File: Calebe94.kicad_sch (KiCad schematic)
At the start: 107 parts, among them J1 USB_B, SW1 SW_DIP_x01, SW10 SW_DIP_x01, SW11 SW_DIP_x01, SW12 SW_DIP_x01, SW13 SW_DIP_x01, SW14 SW_DIP_x01, SW15 SW_DIP_x01, SW16 SW_DIP_x01, SW17 SW_DIP_x01, SW18 SW_DIP_x01, SW19 SW_DIP_x01, SW2 SW_DIP_x01, SW20 SW_DIP_x01, SW21 SW_DIP_x01, SW22 SW_DIP_x01, SW23 SW_DIP_x01, SW24 SW_DIP_x01, SW25 SW_DIP_x01, SW26 SW_DIP_x01, SW27 SW_DIP_x01, SW28 SW_DIP_x01, SW29 SW_DIP_x01, SW3 SW_DIP_x01, SW30 SW_DIP_x01, SW31 SW_DIP_x01, SW32 SW_DIP_x01, SW33 SW_DIP_x01, SW34 SW_DIP_x01, SW35 SW_DIP_x01, SW36 SW_DIP_x01, SW37 SW_DIP_x01, SW38 SW_DIP_x01, SW39 SW_DIP_x01, SW4 SW_DIP_x01, SW40 SW_DIP_x01, SW41 SW_DIP_x01, SW42 SW_DIP_x01, SW43 SW_DIP_x01, SW44 SW_DIP_x01, SW45 SW_DIP_x01, SW46 SW_DIP_x01, SW47 SW_DIP_x01, SW48 SW_DIP_x01, SW49 RESET, SW5 SW_DIP_x01, SW50 BOOT, SW6 SW_DIP_x01, SW7 SW_DIP_x01, SW8 SW_DIP_x01, SW9 SW_DIP_x01, U1 ARDUINO_PRO_MINI

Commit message: Changed routes
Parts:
- SW1: footprint keyboard_parts:ALPS_SKCM_reverse_pad -> keyboard_parts:ALPS_SKCM
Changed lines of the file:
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@@
       (effects (font (size 1.27 1.27)) (justify right))
     )
-    (property "Footprint" "keyboard_parts:ALPS_SKCM_reverse_pad" (id 2) (at 25.4 37.465 0)
+    (property "Footprint" "keyboard_parts:ALPS_SKCM" (id 2) (at 25.4 37.465 0)
       (effects (font (size 1.27 1.27)) hide)
     )
@@
     )
     (path "/c6406fc2-6159-460e-847f-da408c279cb0"
-      (reference "SW1") (unit 1) (value "SW_DIP_x01") (footprint "keyboard_parts:ALPS_SKCM_reverse_pad")
+      (reference "SW1") (unit 1) (value "SW_DIP_x01") (footprint "keyboard_parts:ALPS_SKCM")
     )
     (path "/a06d700f-65f9-46be-b220-6a3499423ba4"

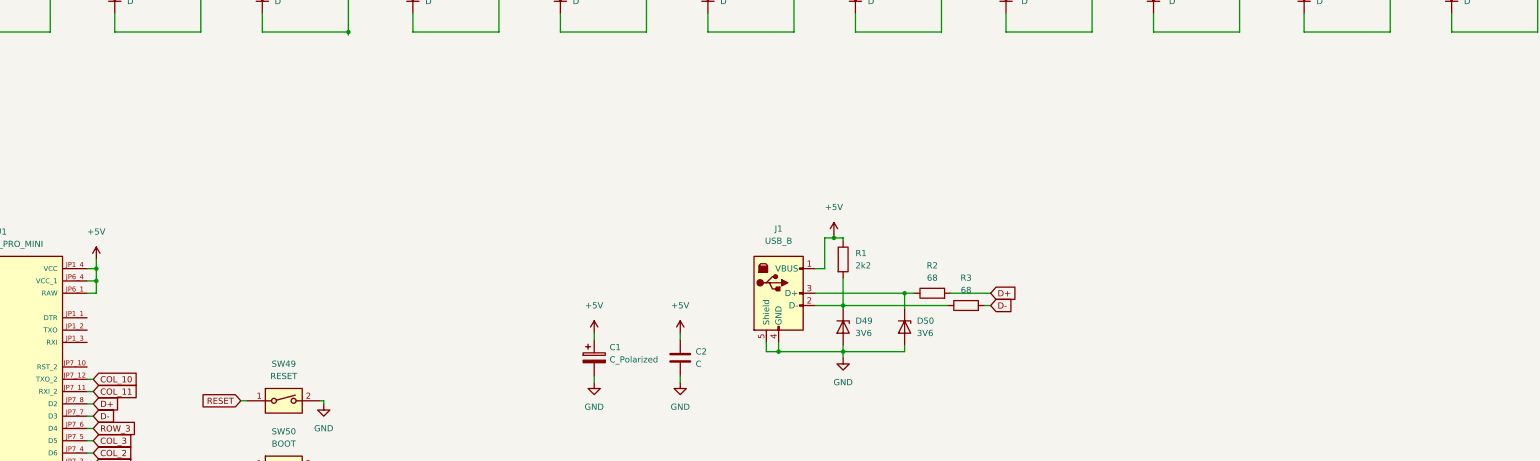
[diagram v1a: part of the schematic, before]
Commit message: Added appa and my logo as silk
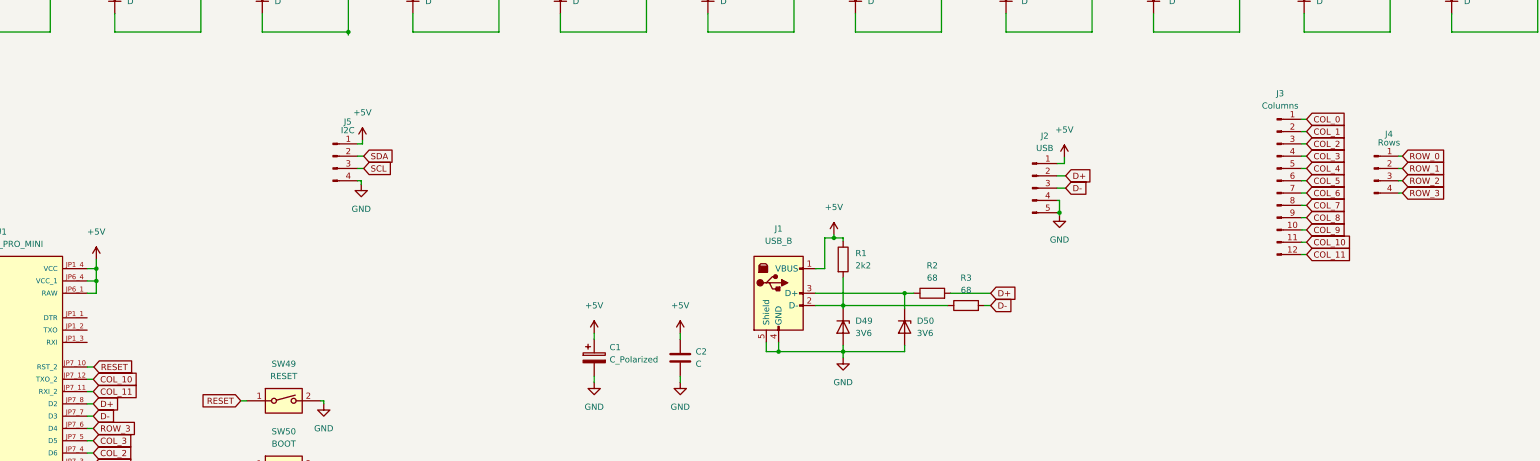
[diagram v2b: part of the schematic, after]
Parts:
- added J2: USB, Connector_PinSocket_2.54mm:PinSocket_1x05_P2.54mm_Vertical, symbol Connector:Conn_01x05_Male
- added J3: Columns, Connector_PinSocket_2.54mm:PinSocket_1x12_P2.54mm_Vertical, symbol Connector:Conn_01x12_Male
- added J4: Rows, Connector_PinSocket_2.54mm:PinSocket_1x04_P2.54mm_Vertical, symbol Connector:Conn_01x04_Male
- added J5: I2C, Connector_PinSocket_2.54mm:PinSocket_1x04_P2.54mm_Vertical, symbol Connector:Conn_01x04_Male
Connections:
- net +5V: now also J2.1 (Pin_1), J5.1 (Pin_1)
- net COL_0: now also J3.1 (Pin_1)
- net COL_1: now also J3.2 (Pin_2)
- net COL_10: now also J3.11 (Pin_11)
- net COL_11: now also J3.12 (Pin_12)
- net COL_2: now also J3.3 (Pin_3)
- net COL_3: now also J3.4 (Pin_4)
- net COL_4: now also J3.5 (Pin_5)
- net COL_5: now also J3.6 (Pin_6)
- net COL_6: now also J3.7 (Pin_7)
- net COL_7: now also J3.8 (Pin_8)
- net COL_8: now also J3.9 (Pin_9)
- net COL_9: now also J3.10 (Pin_10)
- net D+: now also J2.2 (Pin_2)
- net D-: now also J2.3 (Pin_3)
- net GND: now also J2.4 (Pin_4), J2.5 (Pin_5), J5.4 (Pin_4)
- net RESET: now also U1.JP7_10 (RST_2)
- net ROW_0: now also J4.1 (Pin_1)
- net ROW_1: now also J4.2 (Pin_2)
- net ROW_2: now also J4.3 (Pin_3)
- net ROW_3: now also J4.4 (Pin_4)
- net SCL: now also J5.3 (Pin_3)
- net SDA: now also J5.2 (Pin_2)

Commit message: Added gerber folder
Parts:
- added C3, C4: 22p, Capacitor_THT:C_Disc_D3.0mm_W1.6mm_P2.50mm, symbol Device:C
- added C5: C, Capacitor_THT:C_Disc_D4.3mm_W1.9mm_P5.00mm, symbol Device:C
- added J6: ICSP, Connector_PinSocket_2.54mm:PinSocket_2x03_P2.54mm_Vertical, symbol Connector_Generic:Conn_02x03_Counter_Clockwise
- added R4: 10k, Resistor_THT:R_Axial_DIN0204_L3.6mm_D1.6mm_P7.62mm_Horizontal, symbol Device:R
- added U2: ATmega328-P, Package_DIP:DIP-28_W7.62mm, symbol MCU_Microchip_ATmega:ATmega328-P
- added Y1: 16MHz, Crystal:Crystal_HC18-U_Vertical, symbol Device:Crystal
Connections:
- net +5V: now also J6.1 (Pin_1), R4.1, U2.20 (AVCC), U2.7 (VCC)
- net COL_0: now also U2.14 (PB0)
- net COL_1: now also U2.13 (PD7)
- net COL_2: now also U2.12 (PD6)
- net COL_3: now also U2.11 (PD5)
- net COL_4: now also U2.16 (PB2)
- net COL_5: now also U2.15 (PB1)
- net COL_6: now also U2.23 (PC0)
- net COL_7: now also U2.24 (PC1)
- net COL_8: now also U2.25 (PC2)
- net COL_9: now also U2.26 (PC3)
- net D+: now also U2.4 (PD2)
- net D-: now also U2.5 (PD3)
- net GND: now also C3.2, C4.2, C5.2, J6.5 (Pin_5), U2.22 (GND), U2.8 (GND)
- net RESET: now also U1.JP1_1 (DTR), J6.6 (Pin_6), R4.2, U2.1 (~{RESET}/PC6)
- net ROW_1: now also J6.4 (Pin_4), U2.19 (PB5)
- net ROW_3: now also U2.6 (PD4)
- net SCL: now also U2.28 (PC5)
- net SDA: now also U2.27 (PC4)
- net TXD: now reaches U1.JP1_2 (TXO)
- net TXD: now also U2.3 (PD1)
- net RXD: now reaches U1.JP1_3 (RXI)
- net RXD: now also U2.2 (PD0)
- net ROW_0 renamed MISO
- net MISO: now also J6.2 (Pin_2), U2.18 (PB4)
- net ROW_2 renamed MOSI
- net MOSI: now also J6.3 (Pin_3), U2.17 (PB3)
- new net: C5.1, U2.21 (AREF)
- new net XTAL1: C4.1, U2.9 (XTAL1/PB6), Y1.2
- new net XTAL2: C3.1, U2.10 (XTAL2/PB7), Y1.1
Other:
- note added: "This schematic is sort of mirrored and inverted because the "Connector_PinSocket_2.54mm:PinSocket_2x03_P2.54mm_Vertical" is mirrored and inverted."
- moved on the sheet: C1, C2, D49, D50, J1, J2, J3, J4, J5, R1, R2, R3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
